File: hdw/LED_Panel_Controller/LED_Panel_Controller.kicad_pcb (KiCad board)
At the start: 2 copper layers, 595 parts, among them J1201 PIC_UART, J1202 WIFI_UART, J1203 I2C, J1204 WIFI_SPI, J1205 SD_SPI, J1206 FLASH_SPI, J1501 USB_B_Mini, J1701 Micro_SD_Card_Det_Hirose_DM3AT, J1801 WIFI_I2C, J201 +12V IN, J202 Keystone_8191, J203 Keystone_8191, J3301 Panel Data, J3302 Keystone_8191, J3303 Keystone_8191, J801 PICKIT4, Q401 BSS214NW, Q402 ZXMS6004FFTA, Q601 BSS214NW, Q602 ZXMS6004FFTA, Q801 BSS214NW, SW2201 Cap_Touch, SW2202 Cap_Touch, SW801 MRST, U1001 74LVC1G97, U1101 PIC32MZ2048EFG100_IPF, U1201 MCP9804, U1301 LTC1694, U1302 AT24CS32-STUM, U1303 MCP9804, U1401 DS1683, U1501 74LVC1G97, U1502 CP2105, U1503 TXB0104RGY, U1504 TPD3S014DBVR, U1601 INA219BxDCN, U1602 MCP9804, U1701 74LVC1G97, U1702 74LVC1G97, U1801 74LVC1G97, U1802 74LVC1G97, U1803 ATWINC1500-MR210PB, U1901 74LVC1G97, U1902 74LVC1G97, U1903 74LVC1G97, U1904 74LVC1G97, U1905 74LVC1G97, U2001 74LVC1G97, U2002 74LVC1G97, U2003 74LVC1G97, U2004 74LVC1G97, U201 TPS26600RHFT, U2101 DS3231MZ, U2102 TLV6700, U2201 AT42QT1010-TSHR, U2202 AT42QT1010-TSHR, U2203 74LVC1G97, U2204 74LVC1G97, U2301 74LVC1G97, U2302 74LVC1G97, U2303 74LVC1G97, U2304 74LVC1G97, U2305 74LVC1G97, U2306 74LVC1G97, U2307 74LVC1G97, U2308 74LVC1G97, U2401 74LVC1G97, U2402 SST25VF080B-50-4I-S2AF, U2501 74LVC1G97, U2502 SST25VF080B-50-4I-S2AF, U2601 74LVC1G97, U2602 SST25VF080B-50-4I-S2AF, U2701 74LVC1G97, U2702 SST25VF080B-50-4I-S2AF, U2801 74LVC1G97, U2802 SST25VF080B-50-4I-S2AF, U2901 74LVC1G97, U2902 SST25VF080B-50-4I-S2AF, U3001 74LVC1G97, U3002 SST25VF080B-50-4I-S2AF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

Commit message: design rules, hide passive refdes
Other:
- copper layers 2 -> 4
- net class Default: clearance 0.2 -> 0.127; trace_width 0.25 -> 0.254; via_dia 0.8 -> 0.4318; via_drill 0.4 -> 0.2
- net class Power added: clearance 0.127, trace_width 0.635, via_dia 0.4318, via_drill 0.2
- net class Signal added: clearance 0.127, trace_width 0.254, via_dia 0.4318, via_drill 0.2
- rule trace_clearance: 0.2 -> 0.127
- rule trace_min: 0.2 -> 0.0508
- rule via_min_drill: 0.3 -> 0.199898
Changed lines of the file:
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@@
   (page A4)
   (layers
-    (0 F.Cu signal)
-    (31 B.Cu signal)
+    (0 F.Cu mixed)
+    (1 GND mixed)
+    (2 PWR mixed)
+    (31 B.Cu mixed)
     (32 B.Adhes user)
     (33 F.Adhes user)
@@
     (46 B.CrtYd user)
     (47 F.CrtYd user)
-    (48 B.Fab user)
-    (49 F.Fab user)
+    (48 B.Fab user hide)
+    (49 F.Fab user hide)
   )
   (setup
-    (last_trace_width 0.25)
-    (trace_clearance 0.2)
+    (last_trace_width 0.254)
+    (trace_clearance 0.127)
     (zone_clearance 0.508)
     (zone_45_only no)
-    (trace_min 0.2)
-    (via_size 0.8)
-    (via_drill 0.4)
+    (trace_min 0.0508)
+    (via_size 0.4318)
+    (via_drill 0.2)
     (via_min_size 0.4)
-    (via_min_drill 0.3)
+    (via_min_drill 0.199898)
     (uvia_size 0.3)
     (uvia_drill 0.1)
@@
     (uvia_min_size 0.2)
     (uvia_min_drill 0.1)
-    (edge_width 0.05)
+    (edge_width 0.15)
     (segment_width 0.2)
     (pcb_text_width 0.3)
     (pcb_text_size 1.5 1.5)
-    (mod_edge_width 0.12)
+    (mod_edge_width 0.15)
     (mod_text_size 1 1)
     (mod_text_width 0.15)
@@
   (net 371 "Net-(U3202-Pad12)")
   (net_class Default "This is the default net class."
-    (clearance 0.2)
-    (trace_width 0.25)
-    (via_dia 0.8)
-    (via_drill 0.4)
+    (clearance 0.127)
+    (trace_width 0.254)
+    (via_dia 0.4318)
+    (via_drill 0.2)
     (uvia_dia 0.3)
     (uvia_drill 0.1)
+    (diff_pair_width 0.254)
+    (diff_pair_gap 0.127)
+    (add_net B0_POS5)
+  )
+  (net_class Power ""
+    (clearance 0.127)
+    (trace_width 0.635)
+    (via_dia 0.4318)
+    (via_drill 0.2)
+    (uvia_dia 0.3)
+    (uvia_drill 0.1)
+    (add_net GND)
+    (add_net GNDA_MZ)
+    (add_net VBAT)
+  )
+  (net_class Signal ""
+    (clearance 0.127)
+    (trace_width 0.254)
+    (via_dia 0.4318)
+    (via_drill 0.2)
+    (uvia_dia 0.3)
+    (uvia_drill 0.1)
+    (diff_pair_width 0.254)
+    (diff_pair_gap 0.127)
     (add_net +12V)
     (add_net +12Vin)
@@
     (add_net "/WiFi Module/WIFI_VCORE")
     (add_net B0_POS3P3)
-    (add_net B0_POS5)
     (add_net B1_POS3P3)
     (add_net B1_POS5)
@@
     (add_net G1_POS3P3)
     (add_net G1_POS5)
-    (add_net GND)
-    (add_net GNDA_MZ)
     (add_net Heartbeat_LED)
     (add_net I2C_SCL)
@@
     (add_net SD_SPI_SCK)
     (add_net USB_Stream_Mode_LED)
-    (add_net VBAT)
     (add_net VBAT_ADC)
     (add_net VBAT_PGOOD)

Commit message: separated function groups on PCB
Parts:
- removed C1303: 0.1uF, Capacitors_SMD:C_0402
- removed U1303: MCP9804, Package_DFN_QFN:DFN-8-1EP_3x2mm_P0.5mm_EP1.3x1.5mm
- added C913: 0.1uF, Capacitors_SMD:C_0402, F.Cu at (683.3, 81.9)
- added C914: 10uF, Capacitors_SMD:C_0402, F.Cu at (683.3, 84.0)
- added C915: 0.1uF, Capacitors_SMD:C_0402, F.Cu at (686.3, 81.9)
- added C916: 10uF, Capacitors_SMD:C_0402, F.Cu at (686.3, 84.0)
- moved D801 553.5 mm to (632.5, 80.6)
- moved J801 553.5 mm to (608.8, 98.7)
- moved R1101 553.5 mm to (671.9, 79.7)
- moved R1102 553.5 mm to (671.9, 81.9)
- moved R801 553.5 mm to (621.2, 96.3)
- moved R803 553.5 mm to (628.7, 88.3)
- moved C801 553.5 mm to (621.4, 91.9)
- moved C802 553.5 mm to (625.8, 88.2)
- moved L801 553.5 mm to (631.9, 83.7)
- moved L802 553.5 mm to (621.3, 94.1)
- moved Q801 553.5 mm to (622.1, 89.0)
- moved R802 553.5 mm to (631.7, 85.9)
- moved R804 553.5 mm to (624.2, 91.9)
- moved R805 553.5 mm to (636.0, 79.7)
- moved SW801 553.5 mm to (621.9, 80.7)
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
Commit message: some SPI Flash placement
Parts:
- removed the R2406 at (161.8, 51.3)
- removed the R2407 at (158.8, 53.2)
- added C2401: 0.1uF, Capacitors_SMD:C_0402, F.Cu at (240.6, 98.7)
- added C2401: 0.1uF, Capacitors_SMD:C_0402, F.Cu at (240.6, 91.2)
- added C2401: 0.1uF, Capacitors_SMD:C_0402, F.Cu at (240.6, 83.7)
- added C2401: 0.1uF, Capacitors_SMD:C_0402, F.Cu at (240.6, 76.2)
- added C2401: 0.1uF, Capacitors_SMD:C_0402, F.Cu at (240.6, 68.7)
- added C2401: 0.1uF, Capacitors_SMD:C_0402, F.Cu at (240.6, 61.2)
- added C2401: 0.1uF, Capacitors_SMD:C_0402, F.Cu at (240.6, 53.7)
- added C2402: 0.1uF, Capacitors_SMD:C_0402, F.Cu at (250.0, 105.3)
- added C2402: 0.1uF, Capacitors_SMD:C_0402, F.Cu at (250.0, 97.8)
- added C2402: 0.1uF, Capacitors_SMD:C_0402, F.Cu at (250.0, 90.3)
- added C2402: 0.1uF, Capacitors_SMD:C_0402, F.Cu at (250.0, 82.8)
- added C2402: 0.1uF, Capacitors_SMD:C_0402, F.Cu at (250.0, 75.3)
- added C2402: 0.1uF, Capacitors_SMD:C_0402, F.Cu at (250.0, 67.8)
- added C2402: 0.1uF, Capacitors_SMD:C_0402, F.Cu at (250.0, 60.3)
- added D2401: Green, LEDs:LED_0402, F.Cu at (237.7, 100.0)
- added D2401: Green, LEDs:LED_0402, F.Cu at (237.7, 92.5)
- added D2401: Green, LEDs:LED_0402, F.Cu at (237.7, 85.0)
- added D2401: Green, LEDs:LED_0402, F.Cu at (237.7, 77.5)
- added D2401: Green, LEDs:LED_0402, F.Cu at (237.7, 70.0)
- added D2401: Green, LEDs:LED_0402, F.Cu at (237.7, 62.5)
- added D2401: Green, LEDs:LED_0402, F.Cu at (237.7, 55.0)
- added R2401: 1k, Resistors_SMD:R_0402, F.Cu at (237.7, 101.2)
- added R2401: 1k, Resistors_SMD:R_0402, F.Cu at (237.7, 93.7)
- added R2401: 1k, Resistors_SMD:R_0402, F.Cu at (237.7, 86.2)
- added R2401: 1k, Resistors_SMD:R_0402, F.Cu at (237.7, 78.7)
- added R2401: 1k, Resistors_SMD:R_0402, F.Cu at (237.7, 71.2)
- added R2401: 1k, Resistors_SMD:R_0402, F.Cu at (237.7, 63.7)
- added R2401: 1k, Resistors_SMD:R_0402, F.Cu at (237.7, 56.2)
- added R2402: 10, Resistors_SMD:R_0402, F.Cu at (255.7, 103.8)
- added R2402: 10, Resistors_SMD:R_0402, F.Cu at (255.7, 96.3)
- added R2402: 10, Resistors_SMD:R_0402, F.Cu at (255.7, 88.8)
- added R2402: 10, Resistors_SMD:R_0402, F.Cu at (255.7, 81.3)
- added R2402: 10, Resistors_SMD:R_0402, F.Cu at (255.7, 73.8)
- added R2402: 10, Resistors_SMD:R_0402, F.Cu at (255.7, 66.3)
- added R2402: 10, Resistors_SMD:R_0402, F.Cu at (255.7, 58.8)
- added R2403: 10, Resistors_SMD:R_0402, F.Cu at (255.7, 102.5)
- added R2403: 10, Resistors_SMD:R_0402, F.Cu at (255.7, 95.0)
- added R2403: 10, Resistors_SMD:R_0402, F.Cu at (255.7, 87.5)
- added R2403: 10, Resistors_SMD:R_0402, F.Cu at (255.7, 80.0)
- added R2403: 10, Resistors_SMD:R_0402, F.Cu at (255.7, 72.5)
- added R2403: 10, Resistors_SMD:R_0402, F.Cu at (255.7, 65.0)
- added R2403: 10, Resistors_SMD:R_0402, F.Cu at (255.7, 57.5)
- added R2404: 10, Resistors_SMD:R_0402, F.Cu at (244.3, 99.9)
- added R2404: 10, Resistors_SMD:R_0402, F.Cu at (244.3, 92.4)
- added R2404: 10, Resistors_SMD:R_0402, F.Cu at (244.3, 84.9)
- added R2404: 10, Resistors_SMD:R_0402, F.Cu at (244.3, 77.4)
- added R2404: 10, Resistors_SMD:R_0402, F.Cu at (244.3, 69.9)
- added R2404: 10, Resistors_SMD:R_0402, F.Cu at (244.3, 62.4)
- added R2404: 10, Resistors_SMD:R_0402, F.Cu at (244.3, 54.9)
- added R2405: 10k, Resistors_SMD:R_0402, B.Cu at (246.4, 99.9)
- added R2405: 10k, Resistors_SMD:R_0402, B.Cu at (246.4, 92.4)
- added R2405: 10k, Resistors_SMD:R_0402, B.Cu at (246.4, 84.9)
- added R2405: 10k, Resistors_SMD:R_0402, B.Cu at (246.4, 77.4)
- added R2405: 10k, Resistors_SMD:R_0402, B.Cu at (246.4, 69.9)
- added R2405: 10k, Resistors_SMD:R_0402, B.Cu at (246.4, 62.4)
- added R2405: 10k, Resistors_SMD:R_0402, B.Cu at (246.4, 54.9)
- added R2406: 10k, Resistors_SMD:R_0402, B.Cu at (253.6, 102.5)
- added R2406: 10k, Resistors_SMD:R_0402, B.Cu at (253.6, 95.0)
- added R2406: 10k, Resistors_SMD:R_0402, B.Cu at (253.6, 87.5)
- added R2406: 10k, Resistors_SMD:R_0402, B.Cu at (253.6, 80.0)
- added R2406: 10k, Resistors_SMD:R_0402, B.Cu at (253.6, 72.5)
- added R2406: 10k, Resistors_SMD:R_0402, B.Cu at (253.6, 65.0)
- added R2406: 10k, Resistors_SMD:R_0402, B.Cu at (253.6, 57.5)
- added R2406: 10k, Resistors_SMD:R_0402, B.Cu at (253.6, 50.0)
- added R2407: 10k, Resistors_SMD:R_0402, B.Cu at (253.6, 103.8)
- added R2407: 10k, Resistors_SMD:R_0402, B.Cu at (253.6, 96.3)
- added R2407: 10k, Resistors_SMD:R_0402, B.Cu at (253.6, 88.8)
- added R2407: 10k, Resistors_SMD:R_0402, B.Cu at (253.6, 81.3)
- added R2407: 10k, Resistors_SMD:R_0402, B.Cu at (253.6, 73.8)
- added R2407: 10k, Resistors_SMD:R_0402, B.Cu at (253.6, 66.3)
- added R2407: 10k, Resistors_SMD:R_0402, B.Cu at (253.6, 58.8)
- added R2407: 10k, Resistors_SMD:R_0402, B.Cu at (253.6, 51.3)
- added R2408: 10k, Resistors_SMD:R_0402, B.Cu at (246.4, 101.2)
- added R2408: 10k, Resistors_SMD:R_0402, B.Cu at (246.4, 93.7)
- added R2408: 10k, Resistors_SMD:R_0402, B.Cu at (246.4, 86.2)
- added R2408: 10k, Resistors_SMD:R_0402, B.Cu at (246.4, 78.7)
- added R2408: 10k, Resistors_SMD:R_0402, B.Cu at (246.4, 71.2)
- added R2408: 10k, Resistors_SMD:R_0402, B.Cu at (246.4, 63.7)
- added R2408: 10k, Resistors_SMD:R_0402, B.Cu at (246.4, 56.2)
- added R2409: 10, Resistors_SMD:R_0402, F.Cu at (244.3, 101.2)
- added R2409: 10, Resistors_SMD:R_0402, F.Cu at (244.3, 93.7)
- added R2409: 10, Resistors_SMD:R_0402, F.Cu at (244.3, 86.2)
- added R2409: 10, Resistors_SMD:R_0402, F.Cu at (244.3, 78.7)
- added R2409: 10, Resistors_SMD:R_0402, F.Cu at (244.3, 71.2)
- added R2409: 10, Resistors_SMD:R_0402, F.Cu at (244.3, 63.7)
- added R2409: 10, Resistors_SMD:R_0402, F.Cu at (244.3, 56.2)
- added U2401: 74LVC1G97, Package_TO_SOT_SMD:SOT-363_SC-70-6, F.Cu at (240.6, 100.6)
- added U2401: 74LVC1G97, Package_TO_SOT_SMD:SOT-363_SC-70-6, F.Cu at (240.6, 93.1)
- added U2401: 74LVC1G97, Package_TO_SOT_SMD:SOT-363_SC-70-6, F.Cu at (240.6, 85.6)
- added U2401: 74LVC1G97, Package_TO_SOT_SMD:SOT-363_SC-70-6, F.Cu at (240.6, 78.1)
- added U2401: 74LVC1G97, Package_TO_SOT_SMD:SOT-363_SC-70-6, F.Cu at (240.6, 70.6)
- added U2401: 74LVC1G97, Package_TO_SOT_SMD:SOT-363_SC-70-6, F.Cu at (240.6, 63.1)
- added U2401: 74LVC1G97, Package_TO_SOT_SMD:SOT-363_SC-70-6, F.Cu at (240.6, 55.6)
- added U2402: SST25VF080B-50-4I-S2AF, Package_SO:SOIC-8_5.275x5.275mm_P1.27mm, F.Cu at (250.0, 101.9)
- added U2402: SST25VF080B-50-4I-S2AF, Package_SO:SOIC-8_5.275x5.275mm_P1.27mm, F.Cu at (250.0, 94.4)
- added U2402: SST25VF080B-50-4I-S2AF, Package_SO:SOIC-8_5.275x5.275mm_P1.27mm, F.Cu at (250.0, 86.9)
- added U2402: SST25VF080B-50-4I-S2AF, Package_SO:SOIC-8_5.275x5.275mm_P1.27mm, F.Cu at (250.0, 79.4)
- added U2402: SST25VF080B-50-4I-S2AF, Package_SO:SOIC-8_5.275x5.275mm_P1.27mm, F.Cu at (250.0, 71.9)
- added U2402: SST25VF080B-50-4I-S2AF, Package_SO:SOIC-8_5.275x5.275mm_P1.27mm, F.Cu at (250.0, 64.4)
- added U2402: SST25VF080B-50-4I-S2AF, Package_SO:SOIC-8_5.275x5.275mm_P1.27mm, F.Cu at (250.0, 56.9)
- R2405, R2408: moved to B.Cu
- moved U2402 97.7 mm to (250.0, 49.4)
- moved R2403 97.5 mm to (255.7, 50.0)
- moved R2402 94.3 mm to (255.7, 51.3)
- moved R2409 92.1 mm to (244.3, 48.7), turned to 180 degrees
- moved U2401 91.8 mm to (240.6, 48.1), turned to 180 degrees
- moved C2402 91.0 mm to (250.0, 52.8), turned to 180 degrees
- moved R2408 90.9 mm to (246.4, 48.7)
- moved R2404 89.6 mm to (244.3, 47.4), turned to 180 degrees
- moved C2401 88.2 mm to (240.6, 46.2)
- moved R2405 81.9 mm to (246.4, 47.4), turned to 180 degrees
- moved D2401 78.7 mm to (237.7, 47.5), turned to 180 degrees
- moved R2401 75.9 mm to (237.7, 48.7), turned to 180 degrees
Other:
- board outline added: 100 x 100 mm

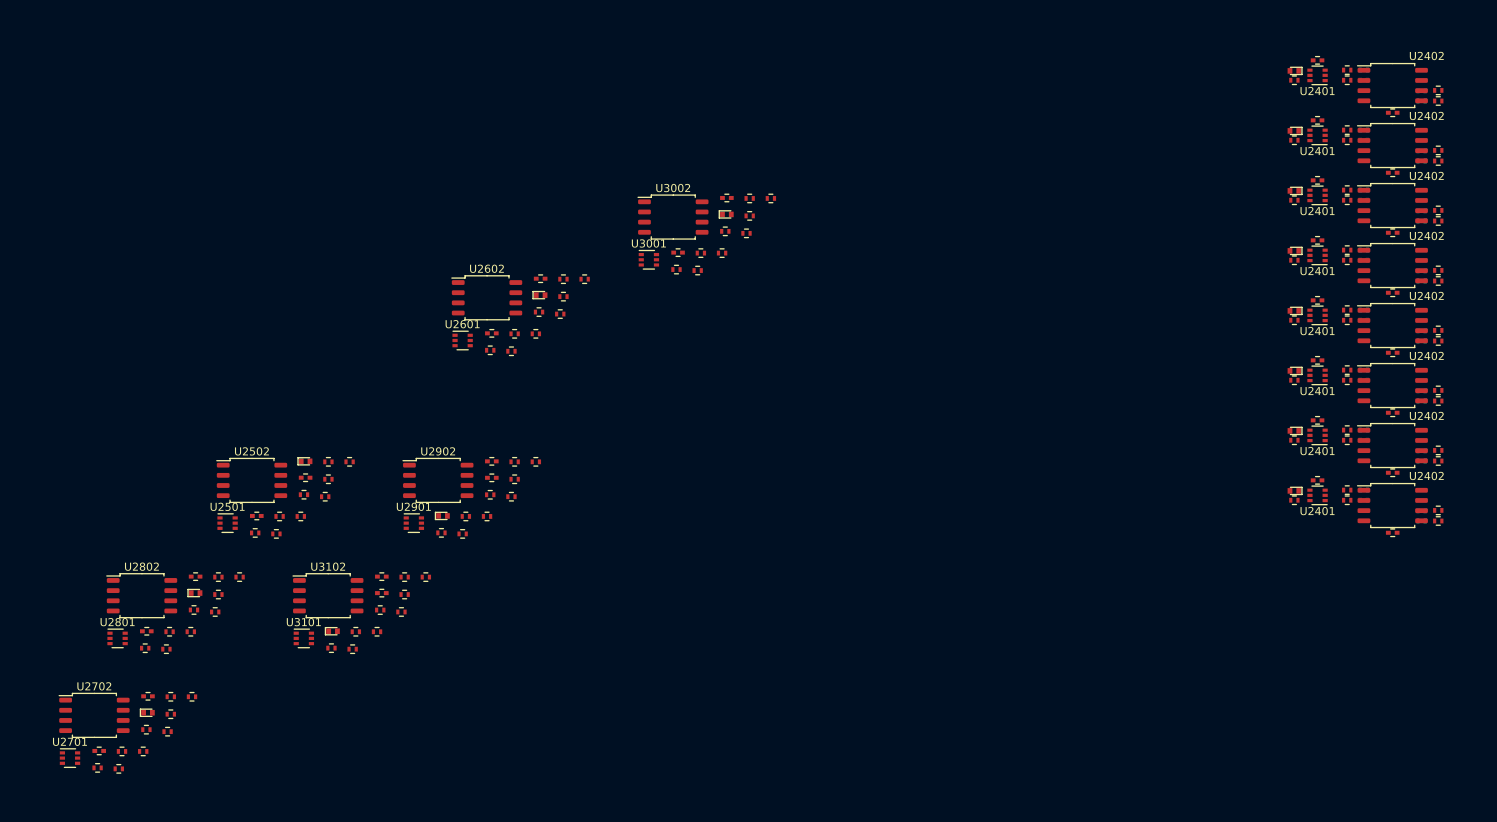
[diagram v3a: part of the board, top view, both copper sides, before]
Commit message: more serial flash layout
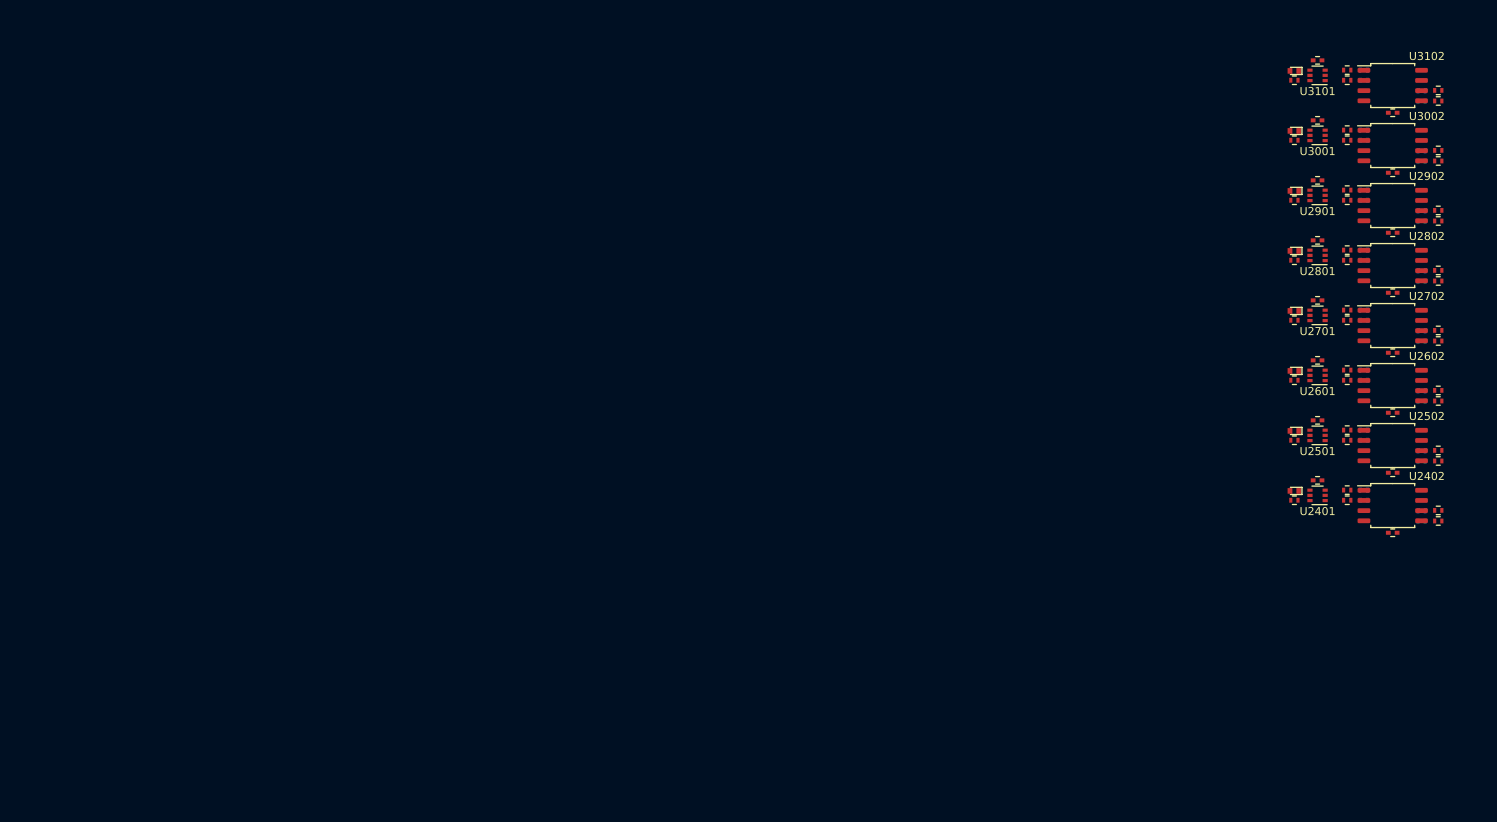
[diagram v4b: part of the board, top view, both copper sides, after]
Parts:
- removed the C2501 at (108.0, 103.2)
- removed the C2502 at (114.1, 98.4)
- removed the C2601 at (143.5, 73.5)
- removed the C2602 at (137.4, 80.4)
- removed the C2701 at (94.4, 125.7)
- removed the C2702 at (88.3, 132.6)
- removed the C2801 at (100.3, 110.8)
- removed the C2802 at (94.2, 117.6)
- removed the C2901 at (137.4, 98.4)
- removed the C2902 at (137.4, 96.4)
- removed the C3001 at (160.7, 70.3)
- removed the C3002 at (166.8, 63.4)
- removed the C3101 at (123.6, 112.8)
- removed the C3102 at (123.6, 110.8)
- removed the D2501 at (114.1, 96.3)
- removed the D2601 at (143.5, 75.6)
- removed the D2701 at (94.4, 127.8)
- removed the D2801 at (100.3, 112.8)
- removed the D2901 at (131.3, 103.2)
- removed the D3001 at (166.8, 65.5)
- removed the D3101 at (117.5, 117.6)
- removed the R2501 at (116.5, 100.8)
- removed the R2502 at (110.4, 105.4)
- removed the R2503 at (113.5, 103.2)
- removed the R2504 at (119.6, 96.4)
- removed the R2505 at (116.9, 98.6)
- removed the R2506 at (113.9, 100.5)
- removed the R2507 at (110.8, 103.2)
- removed the R2508 at (107.8, 105.3)
- removed the R2509 at (116.9, 96.4)
- removed the R2601 at (145.9, 77.9)
- removed the R2602 at (142.9, 80.4)
- removed the R2603 at (139.8, 82.6)
- removed the R2604 at (146.3, 73.6)
- removed the R2605 at (149.0, 73.6)
- removed the R2606 at (146.3, 75.8)
- removed the R2607 at (143.3, 77.7)
- removed the R2608 at (140.2, 80.4)
- removed the R2609 at (137.2, 82.5)
- removed the R2701 at (88.1, 134.7)
- removed the R2702 at (97.2, 125.8)
- removed the R2703 at (91.1, 132.6)
- removed the R2704 at (94.2, 129.9)
- removed the R2705 at (97.2, 128.0)
- removed the R2706 at (99.9, 125.8)
- removed the R2707 at (90.7, 134.8)
- removed the R2708 at (96.8, 130.1)
- removed the R2709 at (93.8, 132.6)
- removed the R2801 at (99.7, 117.7)
- removed the R2802 at (96.7, 119.8)
- removed the R2803 at (102.8, 115.2)
- removed the R2804 at (103.2, 110.8)
- removed the R2805 at (97.1, 117.7)
- removed the R2806 at (100.1, 114.9)
- removed the R2807 at (103.2, 113.0)
- removed the R2808 at (105.8, 110.8)
- removed the R2809 at (94.0, 119.7)
- removed the R2901 at (139.8, 100.8)
- removed the R2902 at (140.2, 96.4)
- removed the R2903 at (131.1, 105.3)
- removed the R2904 at (134.1, 103.2)
- removed the R2905 at (137.2, 100.5)
- removed the R2906 at (140.2, 98.6)
- removed the R2907 at (142.9, 96.4)
- removed the R2908 at (133.7, 105.4)
- removed the R2909 at (136.8, 103.2)
- removed the R3001 at (169.6, 63.5)
- removed the R3002 at (160.5, 72.4)
- removed the R3003 at (163.5, 70.3)
- removed the R3004 at (166.6, 67.6)
- removed the R3005 at (169.6, 65.7)
- removed the R3006 at (172.3, 63.5)
- removed the R3007 at (163.1, 72.5)
- removed the R3008 at (166.2, 70.3)
- removed the R3009 at (169.2, 67.9)
- removed the R3101 at (126.1, 115.2)
- removed the R3102 at (123.0, 117.7)
- removed the R3103 at (120.0, 119.8)
- removed the R3104 at (129.1, 110.8)
- removed the R3105 at (126.5, 113.0)
- removed the R3106 at (123.4, 114.9)
- removed the R3107 at (120.4, 117.7)
- removed the R3108 at (117.3, 119.7)
- removed the R3109 at (126.5, 110.8)
- removed the U2501 at (104.3, 104.1)
- removed the U2502 at (107.4, 98.7)
- removed the U2601 at (133.7, 81.2)
- removed the U2602 at (136.8, 75.9)
- removed the U2701 at (84.6, 133.4)
- removed the U2702 at (87.7, 128.1)
- removed the U2801 at (90.6, 118.5)
- removed the U2802 at (93.6, 113.1)
- removed the U2901 at (127.6, 104.1)
- removed the U2902 at (130.7, 98.7)
- removed the U3001 at (157.0, 71.2)
- removed the U3002 at (160.1, 65.8)
- removed the U3101 at (113.9, 118.5)
- removed the U3102 at (116.9, 113.1)
- renumbered C2401 to C2501, C2402 to C2502, C2401 to C2601, C2402 to C2602, C2401 to C2701, C2402 to C2702, C2401 to C2801, C2402 to C2802, C2401 to C2901, C2402 to C2902, C2401 to C3001, C2402 to C3002, C2401 to C3101, C2402 to C3102, D2401 to D2501, D2401 to D2601, D2401 to D2701, D2401 to D2801, D2401 to D2901, D2401 to D3001, D2401 to D3101, R2401 to R2501, R2402 to R2502, R2403 to R2503, R2404 to R2504, R2405 to R2505, R2406 to R2506, R2407 to R2507, R2408 to R2508, R2409 to R2509, R2401 to R2601, R2402 to R2602, R2403 to R2603, R2404 to R2604, R2405 to R2605, R2406 to R2606, R2407 to R2607, R2408 to R2608, R2409 to R2609, R2401 to R2701, R2402 to R2702, R2403 to R2703, R2404 to R2704, R2405 to R2705, R2406 to R2706, R2407 to R2707, R2408 to R2708, R2409 to R2709, R2401 to R2801, R2402 to R2802, R2403 to R2803, R2404 to R2804, R2405 to R2805, R2406 to R2806, R2407 to R2807, R2408 to R2808, R2409 to R2809, R2401 to R2901, R2402 to R2902, R2403 to R2903, R2404 to R2904, R2405 to R2905, R2406 to R2906, R2407 to R2907, R2408 to R2908, R2409 to R2909, R2401 to R3001, R2402 to R3002, R2403 to R3003, R2404 to R3004, R2405 to R3005, R2406 to R3006, R2407 to R3007, R2408 to R3008, R2409 to R3009, R2401 to R3101, R2402 to R3102, R2403 to R3103, R2404 to R3104, R2405 to R3105, R2406 to R3106, R2407 to R3107, R2408 to R3108, R2409 to R3109, U2401 to U2501, U2402 to U2502, U2401 to U2601, U2402 to U2602, U2401 to U2701, U2402 to U2702, U2401 to U2801, U2402 to U2802, U2401 to U2901, U2402 to U2902, U2401 to U3001, U2402 to U3002, U2401 to U3101, U2402 to U3102
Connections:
- D2501 pad 1: Net-(D2401-Pad1) -> Net-(D2501-Pad1)
- D2501 pad 2: Net-(D2401-Pad2) -> Net-(D2501-Pad2)
- D2601 pad 1: Net-(D2401-Pad1) -> Net-(D2601-Pad1)
- D2601 pad 2: Net-(D2401-Pad2) -> Net-(D2601-Pad2)
- D2701 pad 1: Net-(D2401-Pad1) -> Net-(D2701-Pad1)
- D2701 pad 2: Net-(D2401-Pad2) -> Net-(D2701-Pad2)
- D2801 pad 1: Net-(D2401-Pad1) -> Net-(D2801-Pad1)
- D2801 pad 2: Net-(D2401-Pad2) -> Net-(D2801-Pad2)
- D2901 pad 1: Net-(D2401-Pad1) -> Net-(D2901-Pad1)
- D2901 pad 2: Net-(D2401-Pad2) -> Net-(D2901-Pad2)
- D3001 pad 1: Net-(D2401-Pad1) -> Net-(D3001-Pad1)
- D3001 pad 2: Net-(D2401-Pad2) -> Net-(D3001-Pad2)
- D3101 pad 1: Net-(D2401-Pad1) -> Net-(D3101-Pad1)
- D3101 pad 2: Net-(D2401-Pad2) -> Net-(D3101-Pad2)
- R2501 pad 2: Net-(D2401-Pad2) -> Net-(D2501-Pad2)
- R2502 pad 1: Net-(R2402-Pad1) -> Net-(R2502-Pad1)
- R2503 pad 1: Net-(R2403-Pad1) -> Net-(R2503-Pad1)
- R2504 pad 1: Net-(R2404-Pad1) -> Net-(R2504-Pad1)
- R2504 pad 2: ~FLASH_SPI_CE0 -> ~FLASH_SPI_CE1
- R2505 pad 2: Net-(R2404-Pad1) -> Net-(R2504-Pad1)
- R2506 pad 1: Net-(R2403-Pad1) -> Net-(R2503-Pad1)
- R2507 pad 1: Net-(R2402-Pad1) -> Net-(R2502-Pad1)
- R2508 pad 1: Net-(R2408-Pad1) -> Net-(R2508-Pad1)
- R2509 pad 1: Net-(R2408-Pad1) -> Net-(R2508-Pad1)
- R2601 pad 2: Net-(D2401-Pad2) -> Net-(D2601-Pad2)
- R2602 pad 1: Net-(R2402-Pad1) -> Net-(R2602-Pad1)
- R2603 pad 1: Net-(R2403-Pad1) -> Net-(R2603-Pad1)
- R2604 pad 1: Net-(R2404-Pad1) -> Net-(R2604-Pad1)
- R2604 pad 2: ~FLASH_SPI_CE0 -> ~FLASH_SPI_CE2
- R2605 pad 2: Net-(R2404-Pad1) -> Net-(R2604-Pad1)
- R2606 pad 1: Net-(R2403-Pad1) -> Net-(R2603-Pad1)
- R2607 pad 1: Net-(R2402-Pad1) -> Net-(R2602-Pad1)
- R2608 pad 1: Net-(R2408-Pad1) -> Net-(R2608-Pad1)
- R2609 pad 1: Net-(R2408-Pad1) -> Net-(R2608-Pad1)
- R2701 pad 2: Net-(D2401-Pad2) -> Net-(D2701-Pad2)
- R2702 pad 1: Net-(R2402-Pad1) -> Net-(R2702-Pad1)
- R2703 pad 1: Net-(R2403-Pad1) -> Net-(R2703-Pad1)
- R2704 pad 1: Net-(R2404-Pad1) -> Net-(R2704-Pad1)
- R2704 pad 2: ~FLASH_SPI_CE0 -> ~FLASH_SPI_CE3
- R2705 pad 2: Net-(R2404-Pad1) -> Net-(R2704-Pad1)
- R2706 pad 1: Net-(R2403-Pad1) -> Net-(R2703-Pad1)
- R2707 pad 1: Net-(R2402-Pad1) -> Net-(R2702-Pad1)
- R2708 pad 1: Net-(R2408-Pad1) -> Net-(R2708-Pad1)
- R2709 pad 1: Net-(R2408-Pad1) -> Net-(R2708-Pad1)
- R2801 pad 2: Net-(D2401-Pad2) -> Net-(D2801-Pad2)
- R2802 pad 1: Net-(R2402-Pad1) -> Net-(R2802-Pad1)
- R2803 pad 1: Net-(R2403-Pad1) -> Net-(R2803-Pad1)
- R2804 pad 1: Net-(R2404-Pad1) -> Net-(R2804-Pad1)
- R2804 pad 2: ~FLASH_SPI_CE0 -> ~FLASH_SPI_CE4
- R2805 pad 2: Net-(R2404-Pad1) -> Net-(R2804-Pad1)
- R2806 pad 1: Net-(R2403-Pad1) -> Net-(R2803-Pad1)
- R2807 pad 1: Net-(R2402-Pad1) -> Net-(R2802-Pad1)
- R2808 pad 1: Net-(R2408-Pad1) -> Net-(R2808-Pad1)
- R2809 pad 1: Net-(R2408-Pad1) -> Net-(R2808-Pad1)
- R2901 pad 2: Net-(D2401-Pad2) -> Net-(D2901-Pad2)
- R2902 pad 1: Net-(R2402-Pad1) -> Net-(R2902-Pad1)
- R2903 pad 1: Net-(R2403-Pad1) -> Net-(R2903-Pad1)
- R2904 pad 1: Net-(R2404-Pad1) -> Net-(R2904-Pad1)
- R2904 pad 2: ~FLASH_SPI_CE0 -> ~FLASH_SPI_CE5
- R2905 pad 2: Net-(R2404-Pad1) -> Net-(R2904-Pad1)
- R2906 pad 1: Net-(R2403-Pad1) -> Net-(R2903-Pad1)
- R2907 pad 1: Net-(R2402-Pad1) -> Net-(R2902-Pad1)
- R2908 pad 1: Net-(R2408-Pad1) -> Net-(R2908-Pad1)
- R2909 pad 1: Net-(R2408-Pad1) -> Net-(R2908-Pad1)
- R3001 pad 2: Net-(D2401-Pad2) -> Net-(D3001-Pad2)
- R3002 pad 1: Net-(R2402-Pad1) -> Net-(R3002-Pad1)
- R3003 pad 1: Net-(R2403-Pad1) -> Net-(R3003-Pad1)
- R3004 pad 1: Net-(R2404-Pad1) -> Net-(R3004-Pad1)
- R3004 pad 2: ~FLASH_SPI_CE0 -> ~FLASH_SPI_CE6
- R3005 pad 2: Net-(R2404-Pad1) -> Net-(R3004-Pad1)
- R3006 pad 1: Net-(R2403-Pad1) -> Net-(R3003-Pad1)
- R3007 pad 1: Net-(R2402-Pad1) -> Net-(R3002-Pad1)
- R3008 pad 1: Net-(R2408-Pad1) -> Net-(R3008-Pad1)
- R3009 pad 1: Net-(R2408-Pad1) -> Net-(R3008-Pad1)
- R3101 pad 2: Net-(D2401-Pad2) -> Net-(D3101-Pad2)
- R3102 pad 1: Net-(R2402-Pad1) -> Net-(R3102-Pad1)
- R3103 pad 1: Net-(R2403-Pad1) -> Net-(R3103-Pad1)
- R3104 pad 1: Net-(R2404-Pad1) -> Net-(R3104-Pad1)
- R3104 pad 2: ~FLASH_SPI_CE0 -> ~FLASH_SPI_CE7
- R3105 pad 2: Net-(R2404-Pad1) -> Net-(R3104-Pad1)
- R3106 pad 1: Net-(R2403-Pad1) -> Net-(R3103-Pad1)
- R3107 pad 1: Net-(R2402-Pad1) -> Net-(R3102-Pad1)
- R3108 pad 1: Net-(R2408-Pad1) -> Net-(R3108-Pad1)
- R3109 pad 1: Net-(R2408-Pad1) -> Net-(R3108-Pad1)
- U2501 pad 1: ~FLASH_SPI_CE0 -> ~FLASH_SPI_CE1
- U2501 pad 4: Net-(D2401-Pad1) -> Net-(D2501-Pad1)
- U2502 pad 1: Net-(R2404-Pad1) -> Net-(R2504-Pad1)
- U2502 pad 2: Net-(R2408-Pad1) -> Net-(R2508-Pad1)
- U2502 pad 5: Net-(R2402-Pad1) -> Net-(R2502-Pad1)
- U2502 pad 6: Net-(R2403-Pad1) -> Net-(R2503-Pad1)
- U2601 pad 1: ~FLASH_SPI_CE0 -> ~FLASH_SPI_CE2
- U2601 pad 4: Net-(D2401-Pad1) -> Net-(D2601-Pad1)
- U2602 pad 1: Net-(R2404-Pad1) -> Net-(R2604-Pad1)
- U2602 pad 2: Net-(R2408-Pad1) -> Net-(R2608-Pad1)
- U2602 pad 5: Net-(R2402-Pad1) -> Net-(R2602-Pad1)
- U2602 pad 6: Net-(R2403-Pad1) -> Net-(R2603-Pad1)
- U2701 pad 1: ~FLASH_SPI_CE0 -> ~FLASH_SPI_CE3
- U2701 pad 4: Net-(D2401-Pad1) -> Net-(D2701-Pad1)
- U2702 pad 1: Net-(R2404-Pad1) -> Net-(R2704-Pad1)
- U2702 pad 2: Net-(R2408-Pad1) -> Net-(R2708-Pad1)
- U2702 pad 5: Net-(R2402-Pad1) -> Net-(R2702-Pad1)
- U2702 pad 6: Net-(R2403-Pad1) -> Net-(R2703-Pad1)
- U2801 pad 1: ~FLASH_SPI_CE0 -> ~FLASH_SPI_CE4
- U2801 pad 4: Net-(D2401-Pad1) -> Net-(D2801-Pad1)
- U2802 pad 1: Net-(R2404-Pad1) -> Net-(R2804-Pad1)
- U2802 pad 2: Net-(R2408-Pad1) -> Net-(R2808-Pad1)
- U2802 pad 5: Net-(R2402-Pad1) -> Net-(R2802-Pad1)
- U2802 pad 6: Net-(R2403-Pad1) -> Net-(R2803-Pad1)
- U2901 pad 1: ~FLASH_SPI_CE0 -> ~FLASH_SPI_CE5
- U2901 pad 4: Net-(D2401-Pad1) -> Net-(D2901-Pad1)
- U2902 pad 1: Net-(R2404-Pad1) -> Net-(R2904-Pad1)
- U2902 pad 2: Net-(R2408-Pad1) -> Net-(R2908-Pad1)
- U2902 pad 5: Net-(R2402-Pad1) -> Net-(R2902-Pad1)
- U2902 pad 6: Net-(R2403-Pad1) -> Net-(R2903-Pad1)
- U3001 pad 1: ~FLASH_SPI_CE0 -> ~FLASH_SPI_CE6
- U3001 pad 4: Net-(D2401-Pad1) -> Net-(D3001-Pad1)
- U3002 pad 1: Net-(R2404-Pad1) -> Net-(R3004-Pad1)
- U3002 pad 2: Net-(R2408-Pad1) -> Net-(R3008-Pad1)
- U3002 pad 5: Net-(R2402-Pad1) -> Net-(R3002-Pad1)
- U3002 pad 6: Net-(R2403-Pad1) -> Net-(R3003-Pad1)
- U3101 pad 1: ~FLASH_SPI_CE0 -> ~FLASH_SPI_CE7
- U3101 pad 4: Net-(D2401-Pad1) -> Net-(D3101-Pad1)
- U3102 pad 1: Net-(R2404-Pad1) -> Net-(R3104-Pad1)
- U3102 pad 2: Net-(R2408-Pad1) -> Net-(R3108-Pad1)
- U3102 pad 5: Net-(R2402-Pad1) -> Net-(R3102-Pad1)
- U3102 pad 6: Net-(R2403-Pad1) -> Net-(R3103-Pad1)
